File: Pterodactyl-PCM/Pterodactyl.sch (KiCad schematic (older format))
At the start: 18 parts, among them J1 Left Header, U1 PCM512x

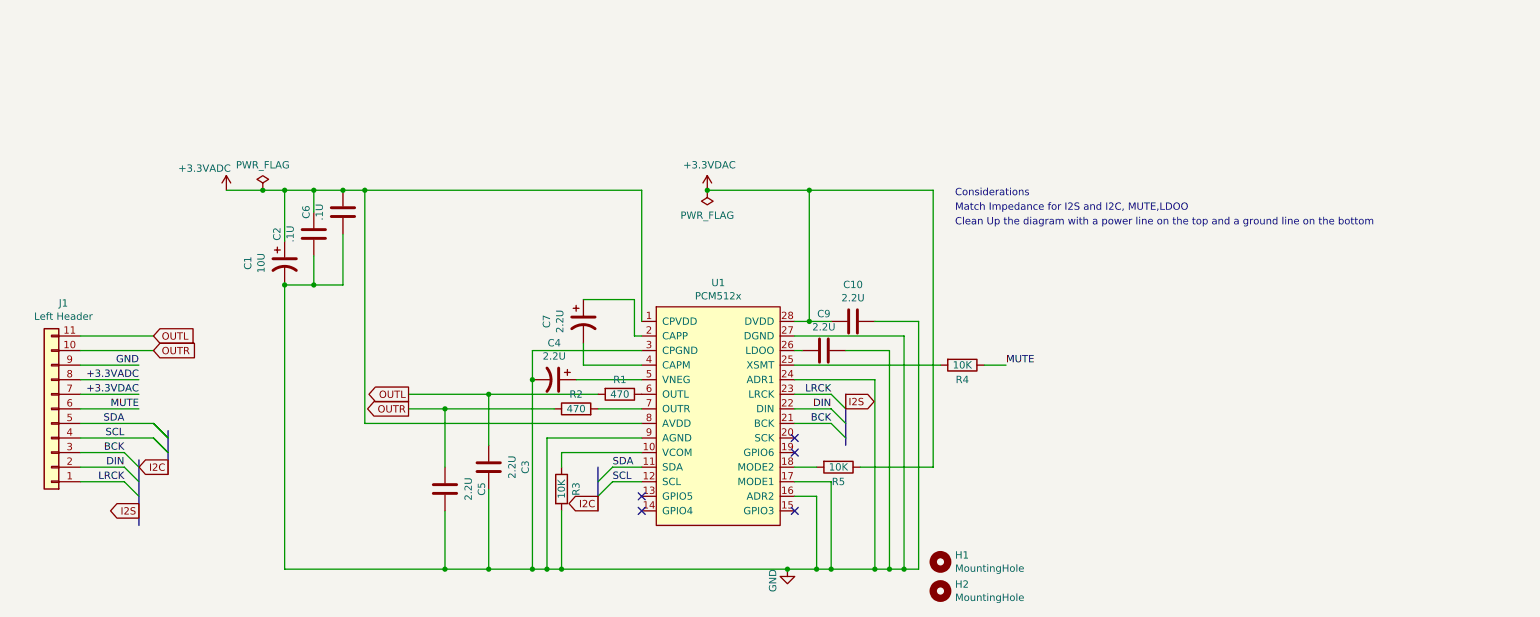
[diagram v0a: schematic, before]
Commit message: added DC regulator
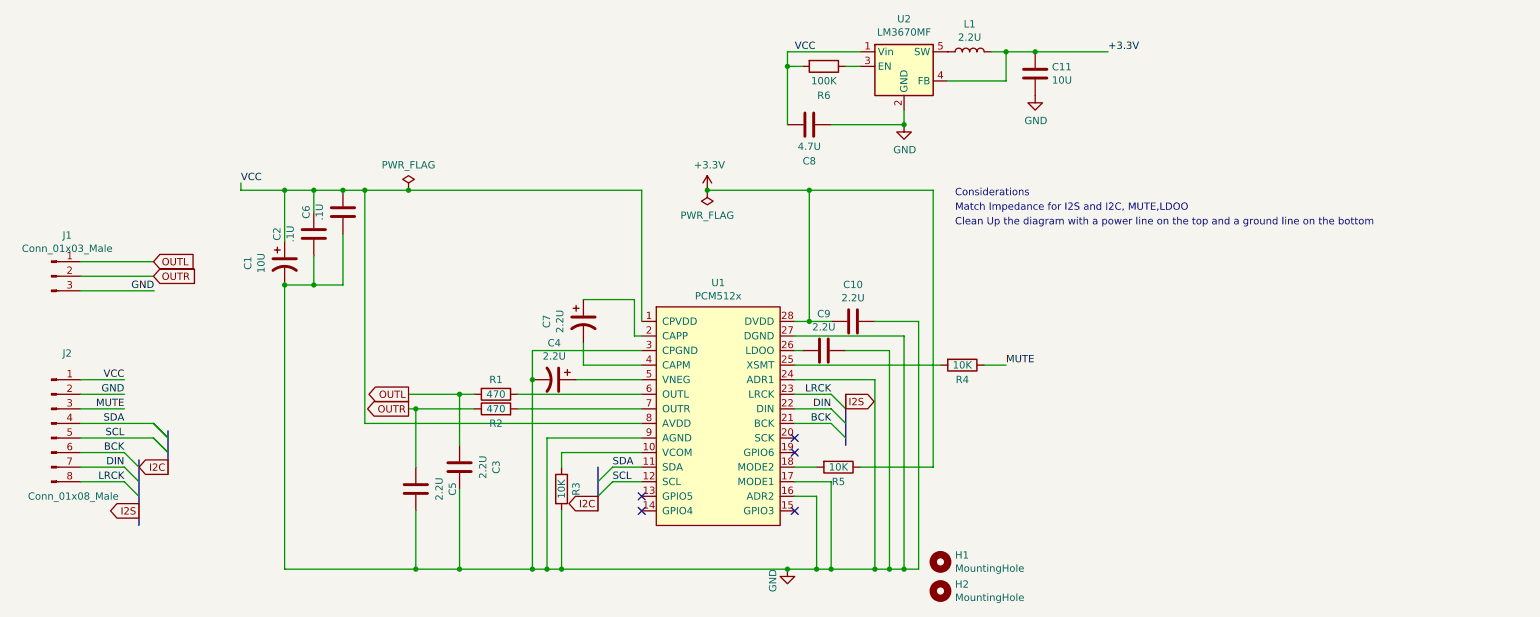
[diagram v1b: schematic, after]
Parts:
- removed J1: Left Header, Connector_PinSocket_2.54mm:PinSocket_1x11_P2.54mm_Vertical, symbol Connector_Generic:Conn_01x11
- added C11: 10U, Capacitor_SMD:CP_Elec_4x4.5, symbol Device:C
- added C8: 4.7U, Capacitor_SMD:CP_Elec_4x4.5, symbol Device:C
- added J1: Conn_01x03_Male, Connector_PinHeader_2.54mm:PinHeader_1x03_P2.54mm_Vertical, symbol Connector:Conn_01x03_Male
- added J2: Conn_01x08_Male, Connector_PinHeader_2.54mm:PinHeader_1x08_P2.54mm_Vertical, symbol Connector:Conn_01x08_Male
- added L1: 2.2U, Inductor_SMD:L_Wuerth_MAPI-3015, symbol Device:L
- added R6: 100K, Resistor_SMD:R_0805_2012Metric_Pad1.20x1.40mm_HandSolder, symbol Device:R
- added U2: LM3670MF, Package_TO_SOT_SMD:TSOT-23-5, symbol Regulator_Switching:LM3670MF
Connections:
- net BCK: now also J2.6 (Pin_6)
- net DIN: now also J2.7 (Pin_7)
- net GND: now also C11.1, C8.2, J1.3 (Pin_3), J2.2 (Pin_2), U2.2 (GND)
- net LRCK: now also J2.8 (Pin_8)
- net MUTE: now also J2.3 (Pin_3)
- net OUTL: now also J1.1 (Pin_1)
- net OUTR: now also J1.2 (Pin_2)
- net SCL: now also J2.5 (Pin_5)
- net SDA: now also J2.4 (Pin_4)
- net +3.3VADC renamed VCC
- net VCC: now also C8.1, J2.1 (Pin_1), R6.2, U2.1 (Vin)
- net +3.3VDAC renamed +3V3
- new net: R6.1, U2.3 (EN)
- new net: L1.1, U2.5 (SW)
- new net +3.3V: C11.2, L1.2, U2.4 (FB)
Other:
- moved on the sheet: C3, C5, R1, R2
